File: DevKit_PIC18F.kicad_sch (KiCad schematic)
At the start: 29 parts, among them J1 PIC_ICSP_ICD, J2 USB_B, J3 5P_UART, J4 RA_PORT, J5 RB_PORT, J6 RD_PORT, J7 RC_PORT, J8 RE_PORT, SW1 SW_DIP, X1 16MHz

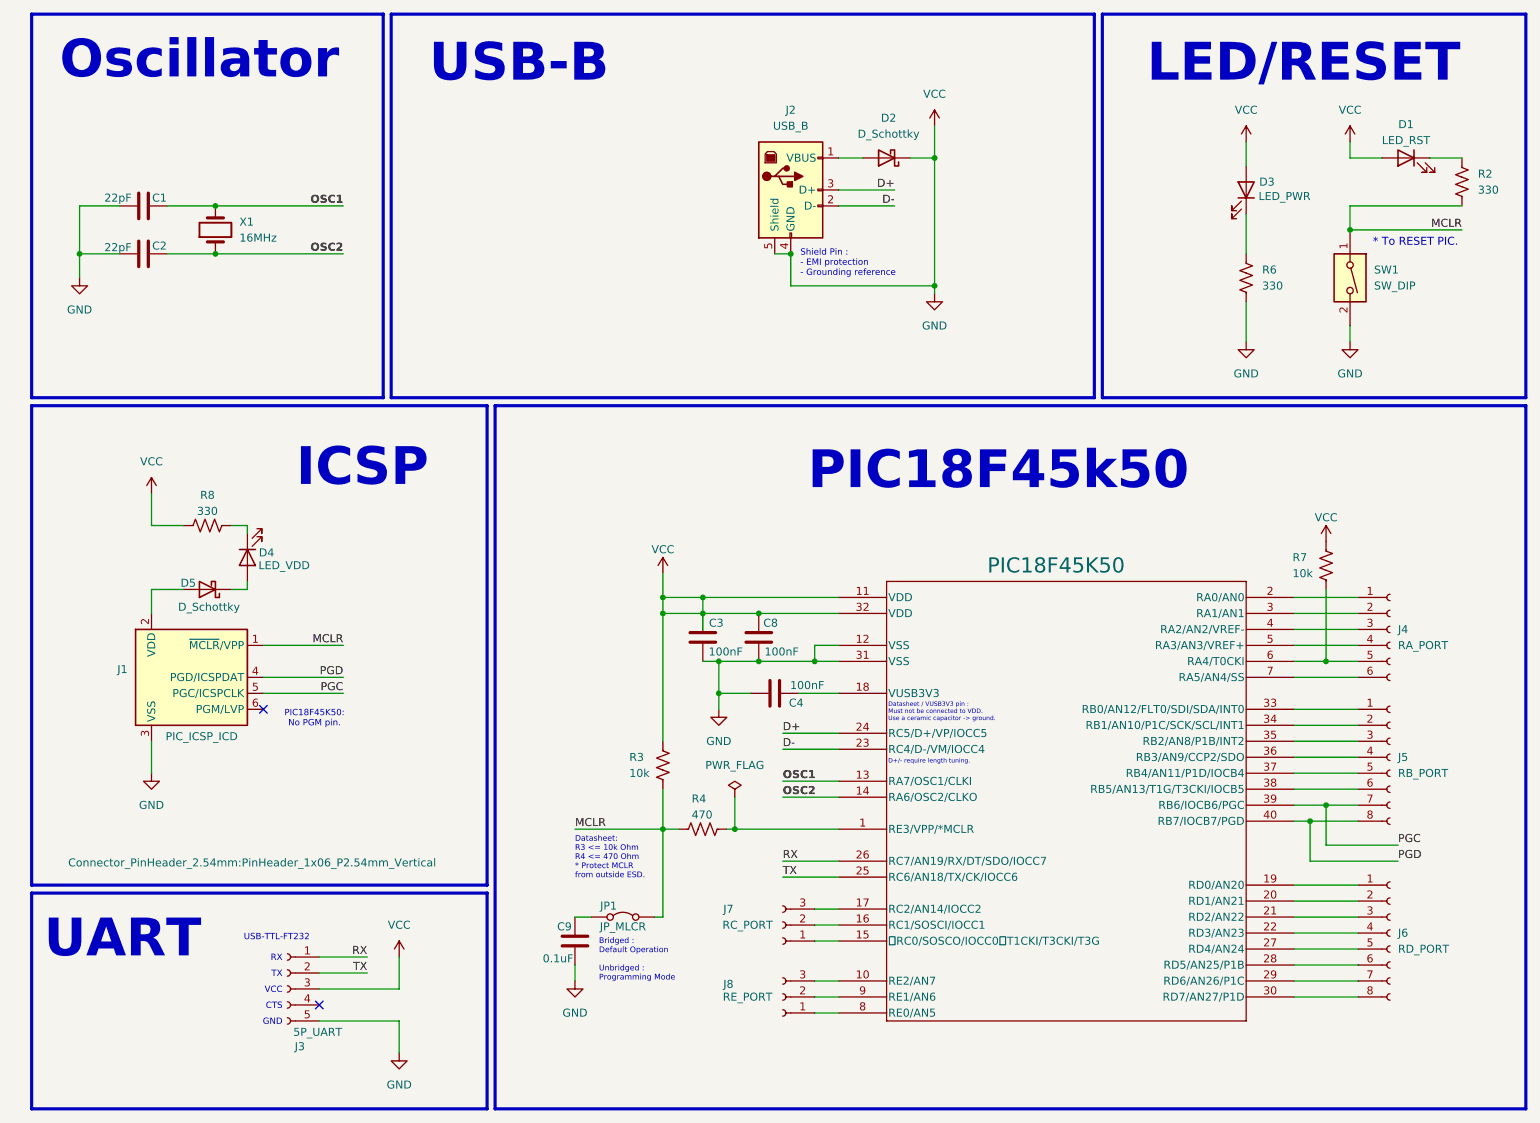
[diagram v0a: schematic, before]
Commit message: Refine/Fix Short-circuit on USB-B
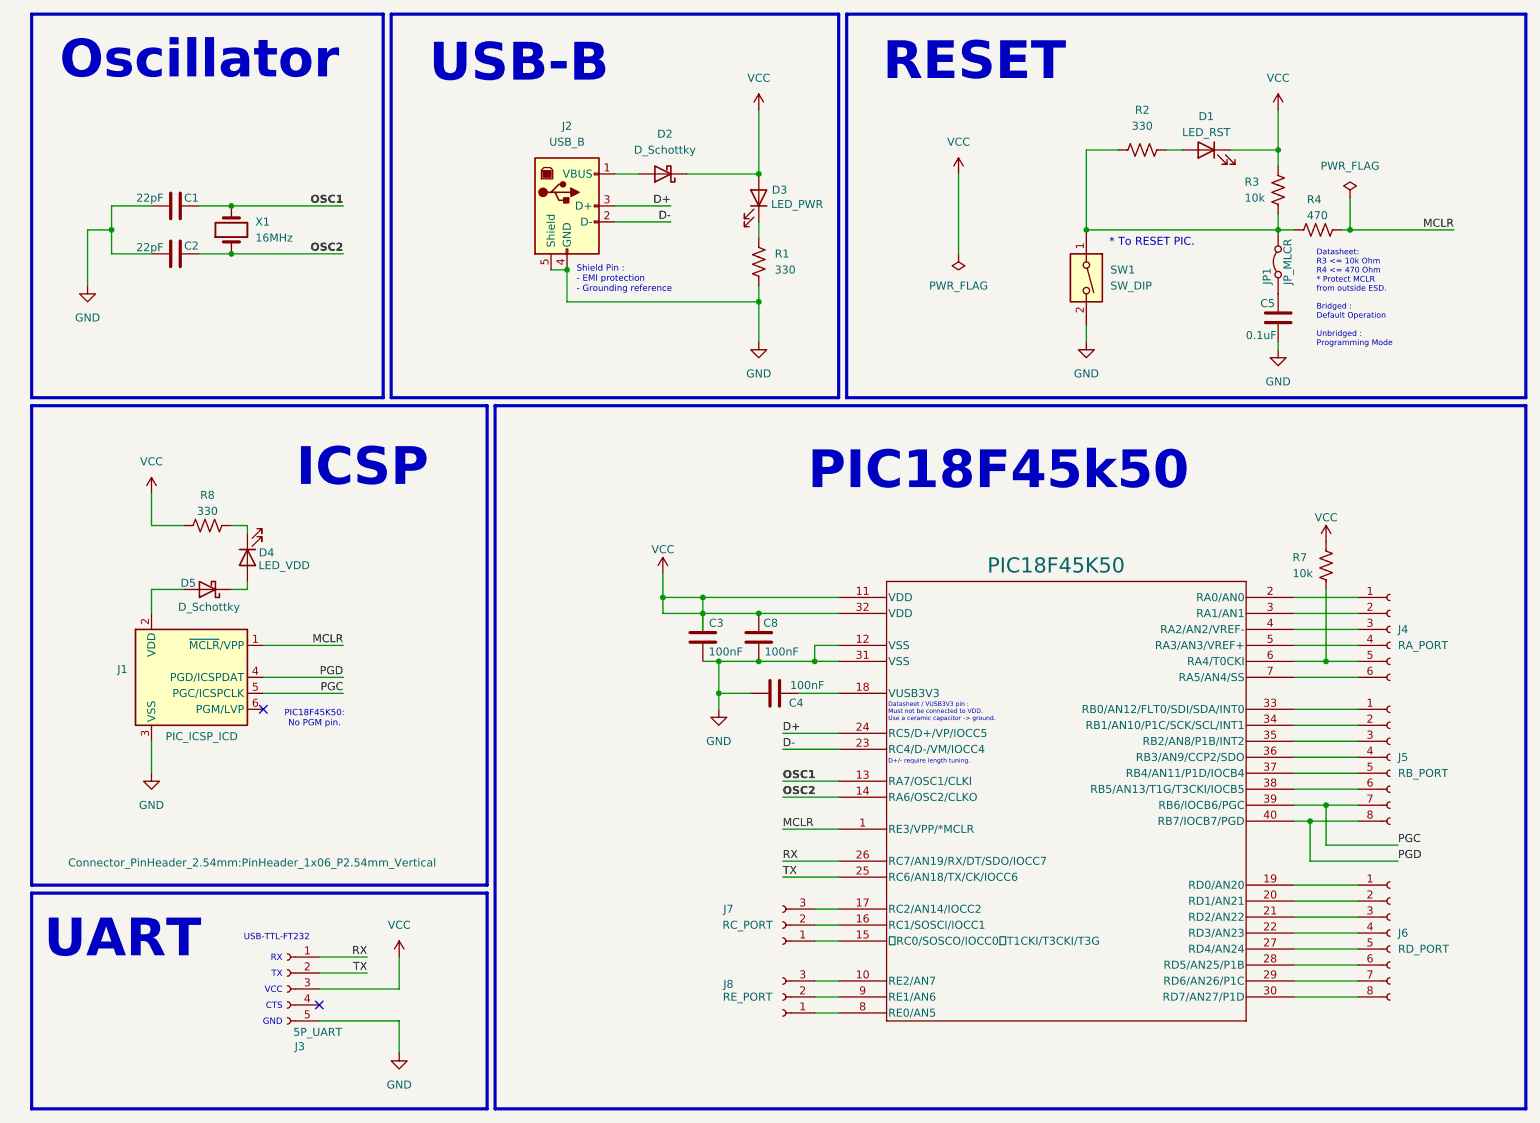
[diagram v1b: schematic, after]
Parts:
- removed C9: 0.1uF, Capacitor_THT:C_Disc_D3.0mm_W1.6mm_P2.50mm, symbol Device:C
- removed R6: 330, Resistor_THT:R_Axial_DIN0204_L3.6mm_D1.6mm_P5.08mm_Horizontal, symbol Device:R_US
- added C5: 0.1uF, Capacitor_THT:C_Disc_D3.0mm_W1.6mm_P2.50mm, symbol Device:C
- added R1: 330, Resistor_THT:R_Axial_DIN0204_L3.6mm_D1.6mm_P5.08mm_Horizontal, symbol Device:R_US
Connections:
- net GND: now also C5.1, R1.2; no longer C3.1, C8.1, D1.2 (A), D2.1 (K), D3.2 (A), J3.3 (Pin_3), PIC18F45K50.11 (VDD), PIC18F45K50.32 (VDD), R3.1, R7.1, R8.1
- net MCLR: now also PIC18F45K50.1 (RE3/VPP/*MCLR), R4.1; no longer JP1.2 (B), R2.2, R3.2, R4.2, SW1.1
- net at JP1.1 (A): now also C5.2
- net at D3.1 (K): now also R1.1
- net at R2.1: now also JP1.2 (B), R3.2, R4.2, SW1.1; no longer D1.1 (K)
- new net: D1.2 (A), R2.2
- new net VCC: C3.1, C8.1, D1.1 (K), D2.1 (K), D3.2 (A), J3.3 (Pin_3), PIC18F45K50.11 (VDD), PIC18F45K50.32 (VDD), R3.1, R7.1, R8.1
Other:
- note added: "RESET"
- note removed: "LED/RESET"
- moved on the sheet: C1, C2, D2, J2, R2, SW1, X1
